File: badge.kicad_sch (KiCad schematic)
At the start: 28 parts, among them J1 SAO V.1.69bis master, Q1 BSS138, SW1 power, SW2 SW_Push, SW3 update epaper, U1 Seeed XIAO ESP32-C3, U2 MH-ET_epaper_ 2.13, U3 5V boost converter, U4 TXS0104EPWR

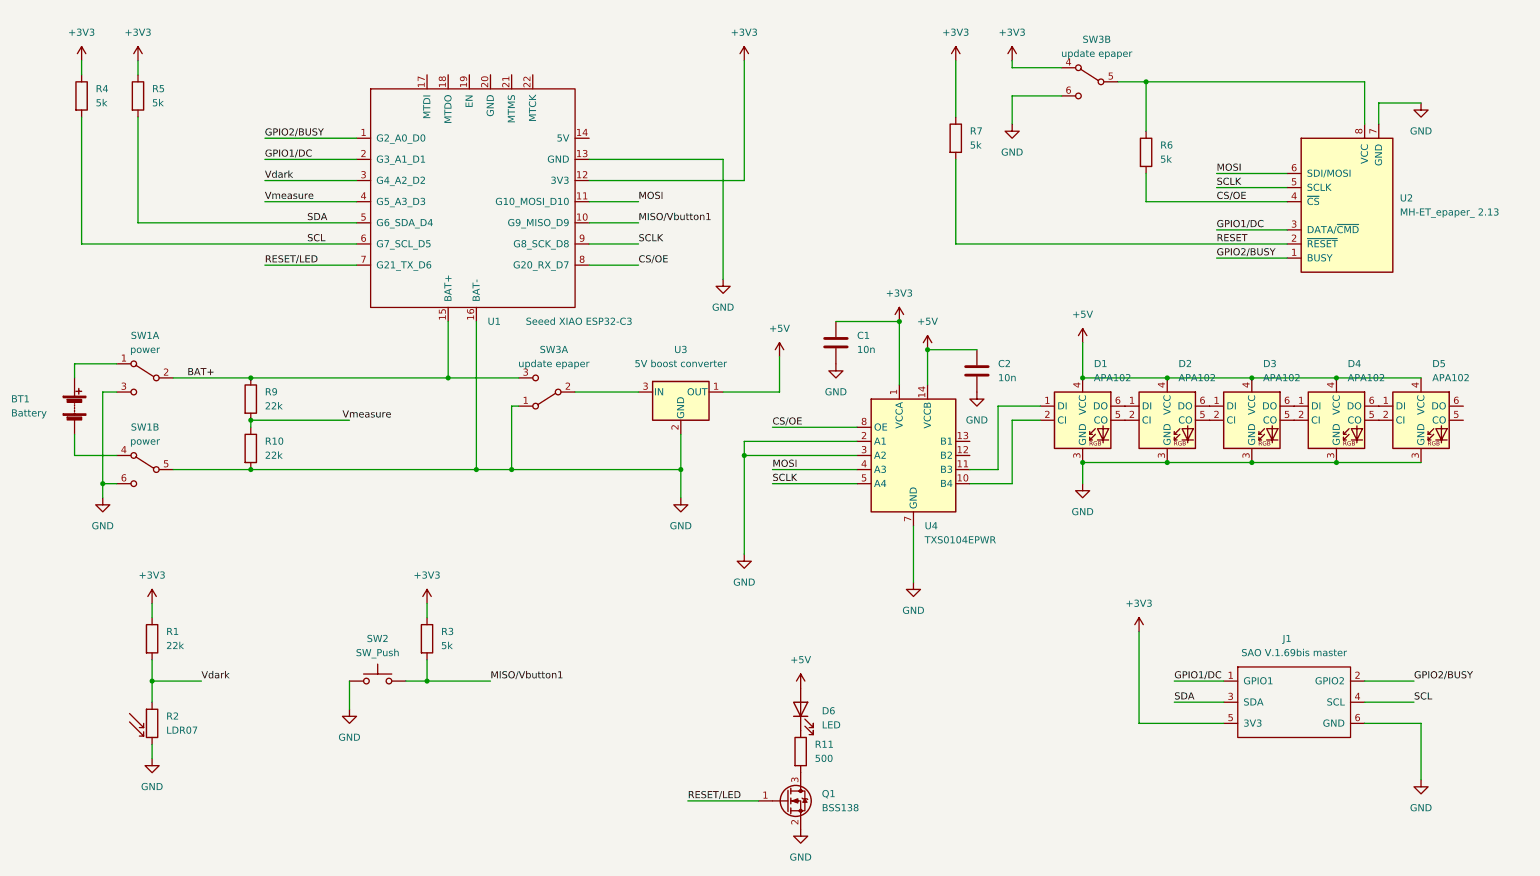
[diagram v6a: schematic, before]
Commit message: finalize resistor values, regenerate Gerbers
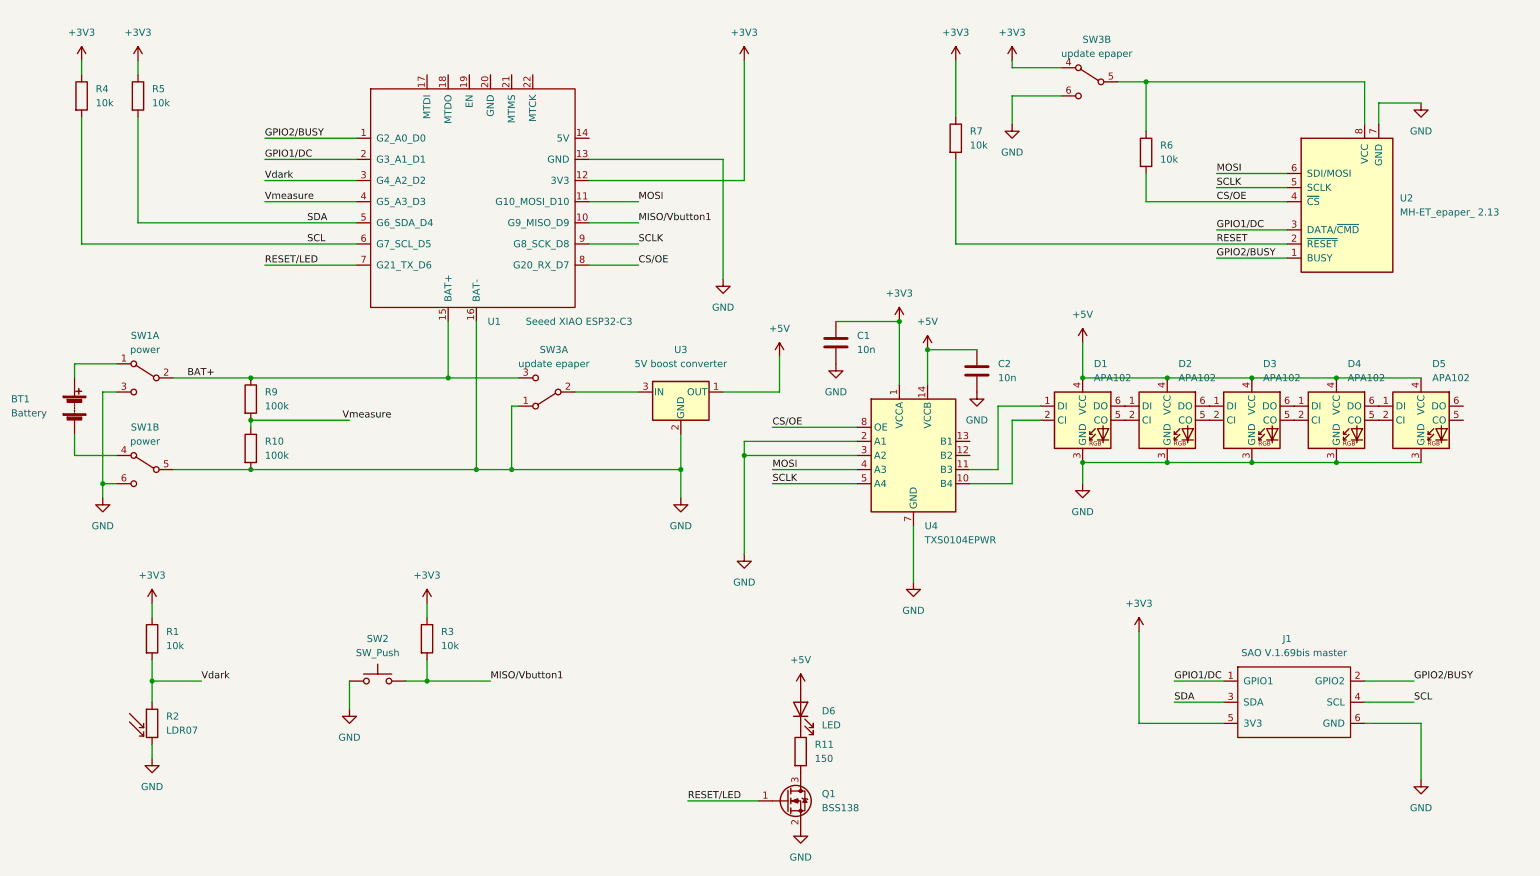
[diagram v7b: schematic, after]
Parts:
- R1: value 22k -> 10k
- R10, R9: value 22k -> 100k
- R11: value 500 -> 150
- R3, R4, R5, R6, R7: value 5k -> 10k
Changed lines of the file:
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@@
       (effects (font (size 1.27 1.27)) (justify left))
     )
-    (property "Value" "5k" (id 1) (at 220.98 41.9099 0)
+    (property "Value" "10k" (id 1) (at 220.98 41.9099 0)
       (effects (font (size 1.27 1.27)) (justify left))
     )
@@
       (effects (font (size 1.27 1.27)) (justify left))
     )
-    (property "Value" "22k" (id 1) (at 59.69 86.3599 0)
+    (property "Value" "100k" (id 1) (at 59.69 86.3599 0)
       (effects (font (size 1.27 1.27)) (justify left))
     )
@@
       (effects (font (size 1.27 1.27)) (justify left))
     )
-    (property "Value" "22k" (id 1) (at 59.69 95.2499 0)
+    (property "Value" "100k" (id 1) (at 59.69 95.2499 0)
       (effects (font (size 1.27 1.27)) (justify left))
     )
@@
       (effects (font (size 1.27 1.27)) (justify left))
     )
-    (property "Value" "5k" (id 1) (at 91.44 129.5399 0)
+    (property "Value" "10k" (id 1) (at 91.44 129.5399 0)
       (effects (font (size 1.27 1.27)) (justify left))
     )
@@
       (effects (font (size 1.27 1.27)) (justify left))
     )
-    (property "Value" "22k" (id 1) (at 41.91 129.5399 0)
+    (property "Value" "10k" (id 1) (at 41.91 129.5399 0)
       (effects (font (size 1.27 1.27)) (justify left))
     )
@@
       (effects (font (size 1.27 1.27)) (justify left))
     )
-    (property "Value" "5k" (id 1) (at 39.37 31.7499 0)
+    (property "Value" "10k" (id 1) (at 39.37 31.7499 0)
       (effects (font (size 1.27 1.27)) (justify left))
     )
@@
       (effects (font (size 1.27 1.27)) (justify left))
     )
-    (property "Value" "500" (id 1) (at 158.75 149.8599 0)
+    (property "Value" "150" (id 1) (at 158.75 149.8599 0)
       (effects (font (size 1.27 1.27)) (justify left))
     )
@@
       (effects (font (size 1.27 1.27)) (justify left))
     )
-    (property "Value" "5k" (id 1) (at 29.21 31.7499 0)
+    (property "Value" "10k" (id 1) (at 29.21 31.7499 0)
       (effects (font (size 1.27 1.27)) (justify left))
     )
@@
       (effects (font (size 1.27 1.27)) (justify left))
     )
-    (property "Value" "5k" (id 1) (at 186.69 39.3699 0)
+    (property "Value" "10k" (id 1) (at 186.69 39.3699 0)
       (effects (font (size 1.27 1.27)) (justify left))
     )
@@
     )
     (path "/51f7f983-853a-452a-8ab7-c02921f8eb56"
-      (reference "R1") (unit 1) (value "22k") (footprint "Resistor_SMD:R_2010_5025Metric_Pad1.40x2.65mm_HandSolder")
+      (reference "R1") (unit 1) (value "10k") (footprint "Resistor_SMD:R_2010_5025Metric_Pad1.40x2.65mm_HandSolder")
     )
     (path "/49c8c0bc-7970-4879-9bd0-eca3704038cf"
@@
     )
     (path "/412d8ef7-b4b1-4b19-8987-16ae2eb34706"
-      (reference "R3") (unit 1) (value "5k") (footprint "Resistor_SMD:R_2010_5025Metric_Pad1.40x2.65mm_HandSolder")
+      (reference "R3") (unit 1) (value "10k") (footprint "Resistor_SMD:R_2010_5025Metric_Pad1.40x2.65mm_HandSolder")
     )
     (path "/98191bdc-fae3-4dad-bf98-01a7b36c38c3"
-      (reference "R4") (unit 1) (value "5k") (footprint "Resistor_SMD:R_2010_5025Metric_Pad1.40x2.65mm_HandSolder")
+      (reference "R4") (unit 1) (value "10k") (footprint "Resistor_SMD:R_2010_5025Metric_Pad1.40x2.65mm_HandSolder")
     )
     (path "/6e8137dd-c5d9-4a87-86a0-351db12a3c4d"
-      (reference "R5") (unit 1) (value "5k") (footprint "Resistor_SMD:R_2010_5025Metric_Pad1.40x2.65mm_HandSolder")
+      (reference "R5") (unit 1) (value "10k") (footprint "Resistor_SMD:R_2010_5025Metric_Pad1.40x2.65mm_HandSolder")
     )
     (path "/10306618-8a84-469d-a7fd-bdec7b390236"
-      (reference "R6") (unit 1) (value "5k") (footprint "Resistor_SMD:R_2010_5025Metric_Pad1.40x2.65mm_HandSolder")
+      (reference "R6") (unit 1) (value "10k") (footprint "Resistor_SMD:R_2010_5025Metric_Pad1.40x2.65mm_HandSolder")
     )
     (path "/c717ce42-ec60-4725-a85e-8a853dd5e35a"
-      (reference "R7") (unit 1) (value "5k") (footprint "Resistor_SMD:R_2010_5025Metric_Pad1.40x2.65mm_HandSolder")
+      (reference "R7") (unit 1) (value "10k") (footprint "Resistor_SMD:R_2010_5025Metric_Pad1.40x2.65mm_HandSolder")
     )
     (path "/24cecee4-9630-4899-9bf5-4f9c803670d0"
-      (reference "R9") (unit 1) (value "22k") (footprint "Resistor_SMD:R_2010_5025Metric_Pad1.40x2.65mm_HandSolder")
+      (reference "R9") (unit 1) (value "100k") (footprint "Resistor_SMD:R_2010_5025Metric_Pad1.40x2.65mm_HandSolder")
     )
     (path "/27089069-07da-431f-91e4-e4a59a574903"
-      (reference "R10") (unit 1) (value "22k") (footprint "Resistor_SMD:R_2010_5025Metric_Pad1.40x2.65mm_HandSolder")
+      (reference "R10") (unit 1) (value "100k") (footprint "Resistor_SMD:R_2010_5025Metric_Pad1.40x2.65mm_HandSolder")
     )
     (path "/71e822d1-6290-4d27-b0af-d53ba7897ba1"
-      (reference "R11") (unit 1) (value "500") (footprint "Resistor_SMD:R_2010_5025Metric_Pad1.40x2.65mm_HandSolder")
+      (reference "R11") (unit 1) (value "150") (footprint "Resistor_SMD:R_2010_5025Metric_Pad1.40x2.65mm_HandSolder")
     )
     (path "/1ad19a07-7043-4709-a6b6-93f957e89d4c"

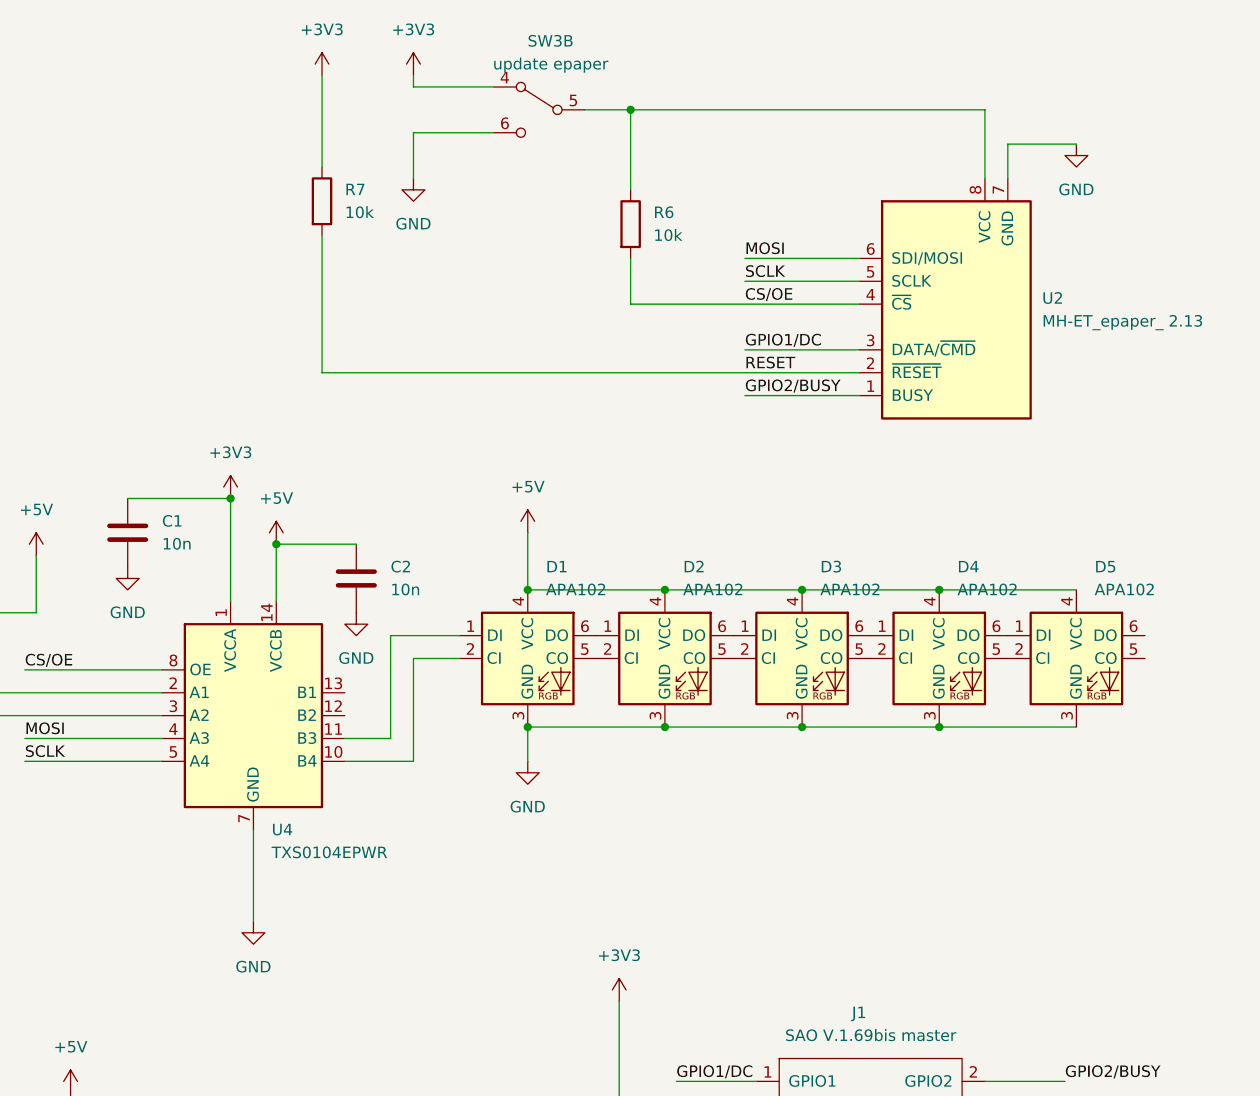
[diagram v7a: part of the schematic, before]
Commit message: fix another whoops - RESET pull-up; add decoupling caps to SmartLEDs
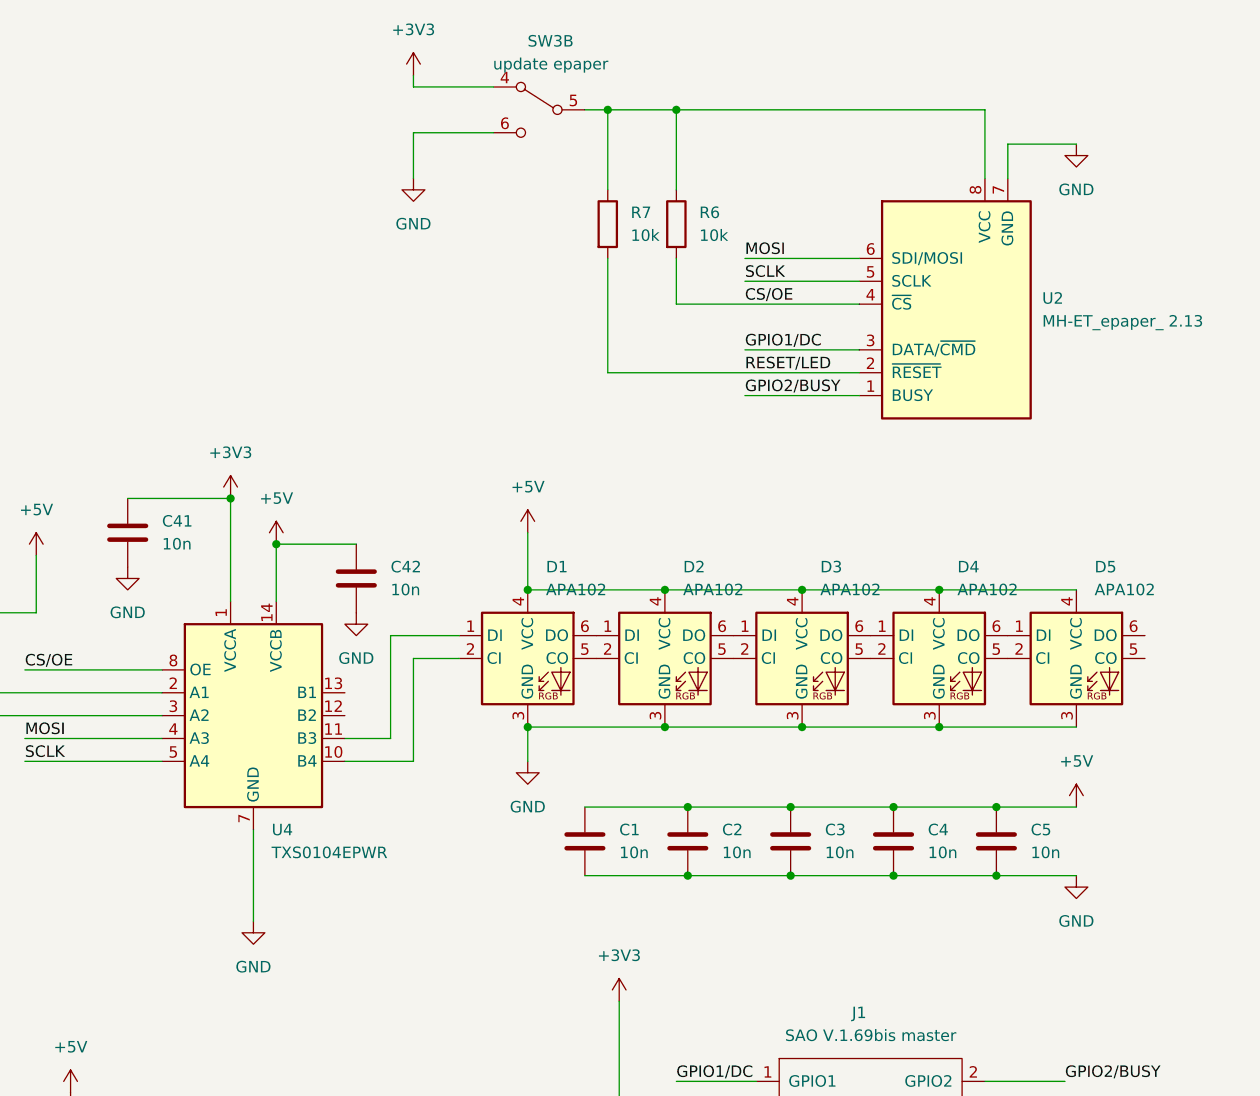
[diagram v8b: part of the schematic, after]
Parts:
- added C1, C2, C3, C4, C5: 10n, Capacitor_SMD:C_1206_3216Metric_Pad1.33x1.80mm_HandSolder, symbol Device:C
- renumbered C1 to C41, C2 to C42
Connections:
- net RESET is gone; now on net RESET/LED: R7.2, U2.2 (~{RESET})
- net +3V3: no longer R7.1
- net +5V: now also C1.1, C2.1, C3.1, C4.1, C5.1
- net GND: now also C1.2, C2.2, C3.2, C4.2, C5.2
- net at R6.1, SW3.5 (B), U2.8 (VCC): now also R7.1
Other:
- moved on the sheet: R6, R7
